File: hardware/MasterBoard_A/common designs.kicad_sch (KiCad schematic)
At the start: 48 parts, among them J12 Conn_01x05_Pin, J13 Main Current Hall Effect Sens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, J14 Conn_02x03_Top_Bottom, Q20 MMBT5550L, Q21 MMBT5550L, Q22 MMBT5550L, U11 IPD70R, U24 LM74502, U25 IPD70R, U42 IPD70R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

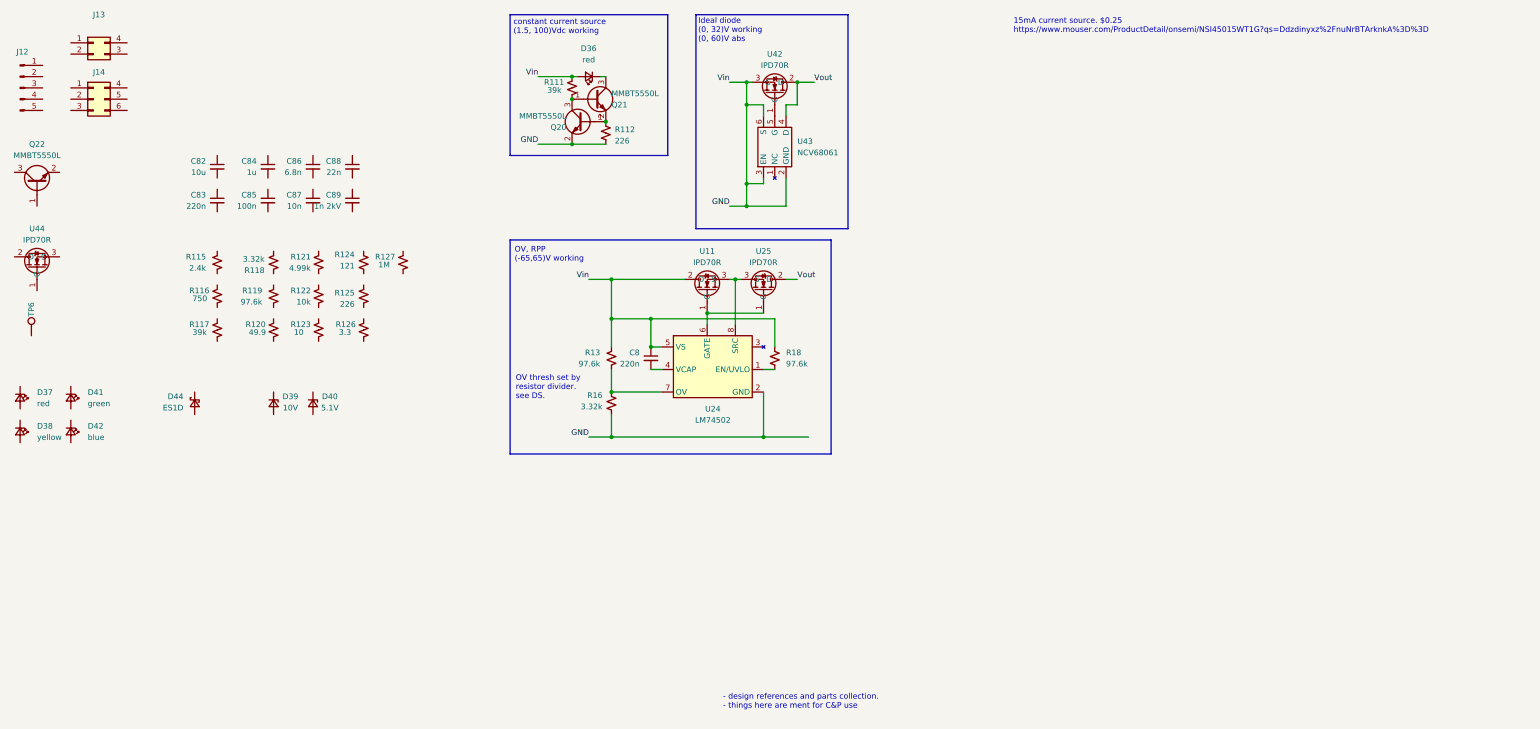
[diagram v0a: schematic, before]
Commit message: better-ified power stuff. new costing program
handy new costing program for kicad. just c&p symbols directly from kicad into it and itll dump out the BOM cost of what ever you gave it
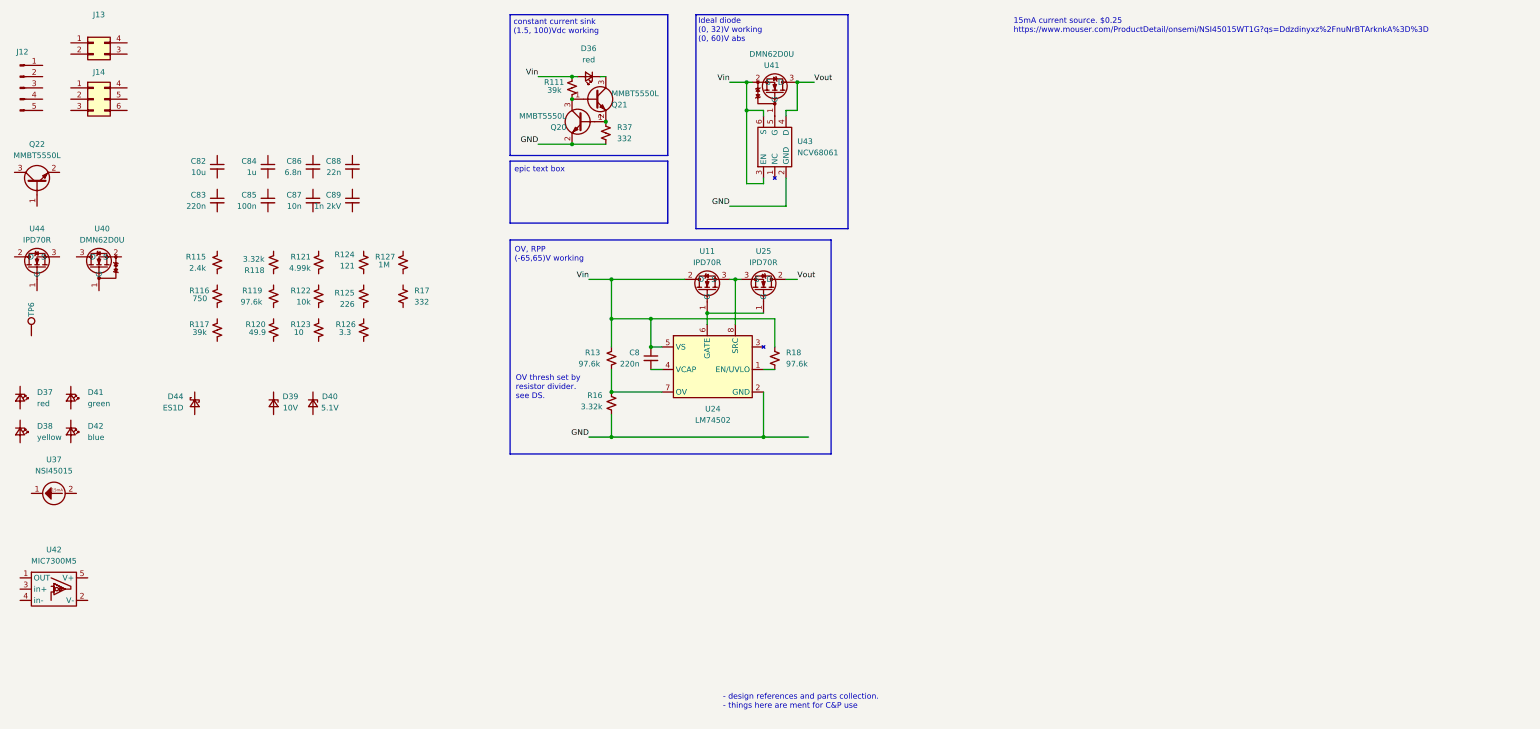
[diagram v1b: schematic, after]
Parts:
- removed R112: 226, Resistor_SMD:R_0805_2012Metric_Pad1.20x1.40mm_HandSolder, symbol Device:R_Small_US
- removed U42: IPD70R, Package_TO_SOT_SMD:TO-252-2, symbol zzLocalLibrary:IPD70R
- added R17, R37: 332, Resistor_SMD:R_1206_3216Metric_Pad1.30x1.75mm_HandSolder, symbol Device:R_Small_US
- added U37: NSI45015, Diode_SMD:D_SOD-123, symbol zzLocalLibrary:NSI45015
- added U40, U41: DMN62D0U, Package_TO_SOT_SMD:SOT-23_Handsoldering, symbol zzLocalLibrary:DMN62D0U
- added U42: MIC7300M5, Package_TO_SOT_SMD:TSOT-23-5_HandSoldering, symbol zzLocalLibrary:MIC7300M5
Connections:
- net GND: now also R37.1; no longer C8.1, D36.2 (A), R111.2, R13.2, R18.2, U11.2 (D), U24.5 (VS), U43.3 (EN), U43.6 (S)
- net Vout: now also U41.3 (D)
- net at U43.5 (G): now also U41.1 (G)
- net at Q20.1 (B), Q21.2 (E): now also R37.2
- new net Vin: C8.1, D36.2 (A), R111.2, R13.2, R18.2, U11.2 (D), U24.5 (VS), U41.2 (S), U43.3 (EN), U43.6 (S)
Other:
- note added: "constant current sink (1.5, 100)Vdc working"
- note removed: "constant current source (1.5, 100)Vdc working"

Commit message: near final
missing direct MCU connections, pin map excel sheet needs piddled with. schematic needs reviewed
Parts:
- added U12: MCP9700x-ETT, Package_TO_SOT_SMD:SOT-23-3, symbol Sensor_Temperature:MCP9700x-ETT
- added U49: TLV713185PDBV, Package_TO_SOT_SMD:SOT-23-5, symbol Regulator_Linear:TLV713185PDBV
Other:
- note added: "- does not go on board. is for convenience - design references and parts collection. - things here are ment for C&P use"
- note removed: "- design references and parts collection. - things here are ment for C&P use"
- note removed: "15mA current source. $0.25 https://www.mouser.com/ProductDetail/onsemi/NSI45015WT1G?qs=Ddzdinyxz%2FnuNrBTArknkA%3D%3D"
- moved on the sheet: C8, R13, R16, R18, U11, U24, U25, U41, U42, U43

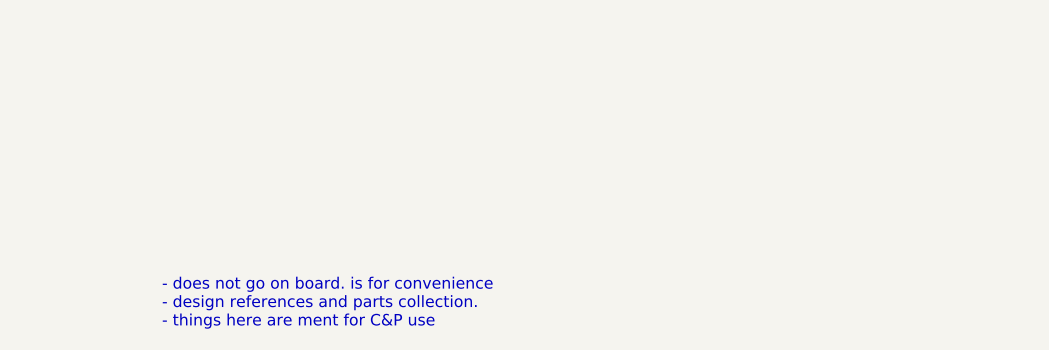
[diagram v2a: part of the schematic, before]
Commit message: one must have hope
eyeballed the ethernet transmission lines, i think it'll work. absolute pain without using footprints smaller than 0805 but it think itll be fine. also shuffled together the PWM sig bank
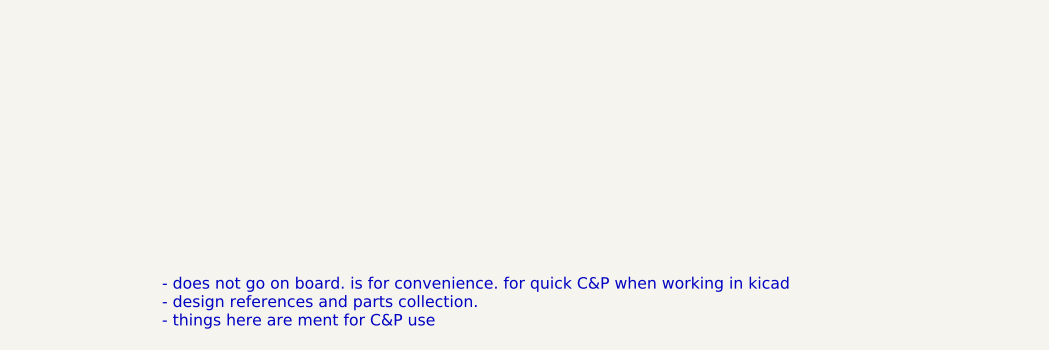
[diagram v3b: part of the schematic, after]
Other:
- note added: "- does not go on board. is for convenience. for quick C&P when working in kicad - design references and parts collection. - things here are ment for C&P use"
- note removed: "- does not go on board. is for convenience - design references and parts collection. - things here are ment for C&P use"

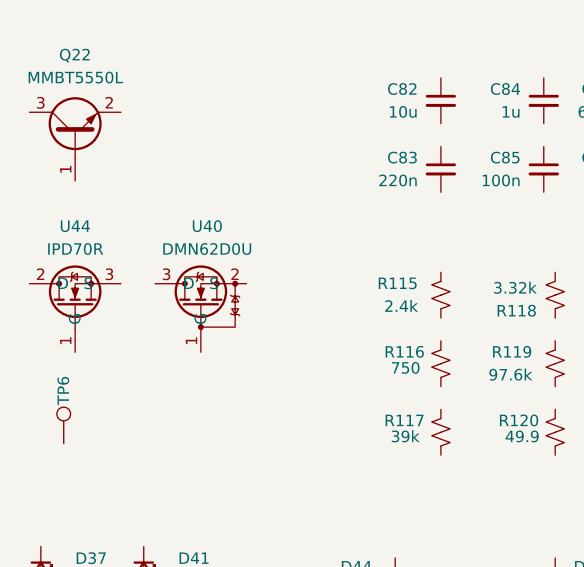
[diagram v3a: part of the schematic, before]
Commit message: partial layout of psu
pdn about to look like a mine field
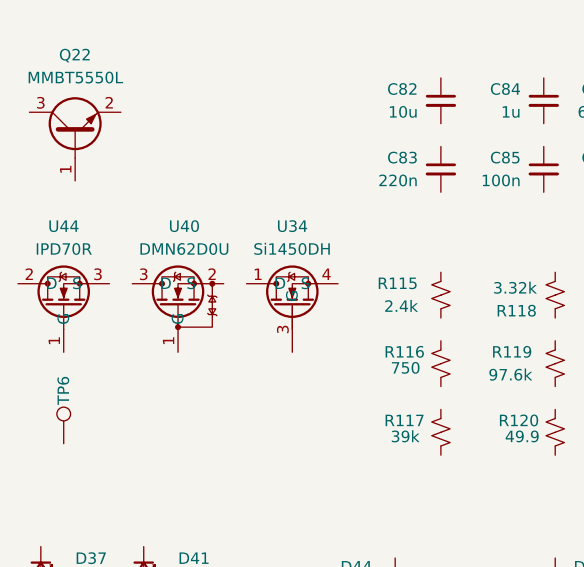
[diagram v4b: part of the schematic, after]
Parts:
- added U34: Si1450DH, Package_TO_SOT_SMD:SOT-363_SC-70-6_Handsoldering, symbol zzLocalLibrary:Si1480DH
- U43: footprint Package_SO:TSOP-6_1.65x3.05mm_P0.95mm -> Package_TO_SOT_SMD:TSOT-23-6
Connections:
- new net: U34.1 (D), U34.2 (D), U34.5 (D), U34.6 (D)
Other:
- moved on the sheet: U40, U44
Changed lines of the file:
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@@
 	)
 	(symbol
+		(lib_id "zzLocalLibrary:Si1480DH")
+		(at 48.26 66.04 0)
+		(unit 1)
+		(exclude_from_sim no)
+		(in_bom yes)
+		(on_board yes)
+		(dnp no)
+		(fields_autoplaced yes)
+		(property "Reference" "U34"
+			(at 48.26 63.5 0)
+			(effects
+				(font
+					(size 1.27 1.27)
+				)
+			)
+		)
+		(property "Value" "Si1450DH"
+			(at 48.26 66.04 0)
+			(effects
+				(font
+					(size 1.27 1.27)
+				)
+			)
+		)
+		(property "Footprint" "Package_TO_SOT_SMD:SOT-363_SC-70-6_Handsoldering"
+			(at 48.26 66.04 0)
+			(effects
+				(font
+					(size 1.27 1.27)
+				)
+				(hide yes)
+			)
+		)
+		(property "Datasheet" "https://www.vishay.com/docs/67327/si1480dh.pdf"
+			(at 48.26 66.04 0)
+			(effects
+				(font
+					(size 1.27 1.27)
+				)
+				(hide yes)
+			)
+		)
+		(property "Description" ""
+			(at 48.26 66.04 0)
+			(effects
+				(font
+					(size 1.27 1.27)
+				)
+				(hide yes)
+			)
+		)
+		(property "specs" "2.6A cont, 200mOhm, 100Vds, +-20Vgs, -55C, +150C"
+			(at 48.26 66.04 0)
+			(effects
+				(font
+					(size 1.27 1.27)
+				)
+				(hide yes)
+			)
+		)
+		(property "mouser" "https://www.mouser.com/ProductDetail/Vishay-Siliconix/SI1480DH-T1-BE3?qs=zW32dvEIR3scWOH7DHfYCg%3D%3D"
+			(at 48.26 66.04 0)
+			(effects
+				(font
+					(size 1.27 1.27)
+				)
+				(hide yes)
+			)
+		)
+		(property "unit x10" "0.274"
+			(at 48.26 66.04 0)
+			(effects
+				(font
+					(size 1.27 1.27)
+				)
+				(hide yes)
+			)
+		)
+		(property "unit x1" "0.34"
+			(at 48.26 66.04 0)
+			(effects
+				(font
+					(size 1.27 1.27)
+				)
+				(hide yes)
+			)
+		)
+		(pin "5"
+		)
+		(pin "4"
+		)
+		(pin "3"
+		)
+		(pin "2"
+		)
+		(pin "1"
+		)
+		(pin "6"
+		)
+		(instances
+			(project "MasterBoard_A"
+				(path "/20ac6af0-79b5-4ba6-aad3-75081d02c913/e647e6c7-d2c9-4086-bd05-45f6d07d327b"
+					(reference "U34")
+					(unit 1)
+				)
+			)
+		)
+	)
+	(symbol
 		(lib_id "zzLocalLibrary:NSI45015")
 		(at 27.94 121.92 0)
@@
 	(symbol
 		(lib_id "zzLocalLibrary:DMN62D0U")
-		(at 38.1 69.85 90)
+		(at 35.56 69.85 90)
 		(unit 1)
 		(exclude_from_sim no)
@@
 		(fields_autoplaced yes)
 		(property "Reference" "U40"
-			(at 38.7985 63.5 90)
+			(at 36.2585 63.5 90)
 			(effects
 				(font
@@
 		)
 		(property "Value" "DMN62D0U"
-			(at 38.7985 66.04 90)
+			(at 36.2585 66.04 90)
 			(effects
 				(font
@@
 		)
 		(property "Footprint" "Package_TO_SOT_SMD:SOT-23_Handsoldering"
-			(at 38.1 69.85 0)
+			(at 35.56 69.85 0)
 			(effects
 				(font
@@
 		)
 		(property "Datasheet" "https://4donline.ihs.com/images/VipMasterIC/IC/DIOD/DIOD-S-A0002833665/DIOD-S-A0002833270-1.pdf?hkey=CECEF36DEECDED6468708AAF2E19C0C6"
-			(at 38.1 69.85 0)
+			(at 35.56 69.85 0)
 			(effects
 				(font
@@
 		)
 		(property "Description" ""
-			(at 38.1 69.85 0)
+			(at 35.56 69.85 0)
 			(effects
 				(font
@@
 		)
 		(property "specs" "500mVth, 60Vds, +-20Vgs, 380mA cont, 2 ohm, 590mW"
-			(at 38.1 69.85 0)
+			(at 35.56 69.85 0)
 			(effects
 				(font
@@
 		)
 		(property "mouser" "https://www.mouser.com/ProductDetail/Diodes-Incorporated/DMN62D0U-7?qs=ANipbH0jDF1YQ7DvWYjVRw%3D%3D"
-			(at 38.1 69.85 0)
+			(at 35.56 69.85 0)
 			(effects
 				(font
@@
 		)
 		(property "unit x10" "0.102"
-			(at 38.1 69.85 0)
+			(at 35.56 69.85 0)
 			(effects
 				(font
@@
 		)
 		(property "unit x1" "0.12"
-			(at 38.1 69.85 0)
+			(at 35.56 69.85 0)
 			(effects
 				(font
@@
 		)
 		(property "Sim.Pins" ""
-			(at 38.1 69.85 90)
+			(at 35.56 69.85 90)
 			(effects
 				(font
@@
 		)
 		(property "note" ""
-			(at 38.1 69.85 90)
+			(at 35.56 69.85 90)
 			(effects
 				(font
@@
 			)
 		)
-		(property "Footprint" "Package_SO:TSOP-6_1.65x3.05mm_P0.95mm"
+		(property "Footprint" "Package_TO_SOT_SMD:TSOT-23-6"
 			(at 185.42 44.45 0)
 			(effects
@@
 	(symbol
 		(lib_id "zzLocalLibrary:IPD70R")
-		(at 24.13 69.85 90)
+		(at 22.86 69.85 90)
 		(unit 1)
 		(exclude_from_sim no)
@@
 		(fields_autoplaced yes)
 		(property "Reference" "U44"
-			(at 24.13 63.5 90)
+			(at 22.86 63.5 90)
 			(effects
 				(font
@@
 		)
 		(property "Value" "IPD70R"
-			(at 24.13 66.04 90)
+			(at 22.86 66.04 90)
 			(effects
 				(font
@@
 		)
 		(property "Footprint" "Package_TO_SOT_SMD:TO-252-2"
-			(at 24.13 69.85 0)
+			(at 22.86 69.85 0)
 			(effects
 				(font
@@
 		)
 		(property "Datasheet" ""
-			(at 24.13 69.85 0)
+			(at 22.86 69.85 0)
 			(effects
 				(font
@@
 		)
 		(property "Description" "nmos, 300mOhm, 700Vdc, 2.5 [16,-16]Vgs, -40C,+150C"
-			(at 24.13 69.85 0)
+			(at 22.86 69.85 0)
 			(effects
 				(font
@@
 		)
 		(property "mouser" "https://www.mouser.com/ProductDetail/Infineon-Technologies/IPD70R360P7SAUMA1?qs=KuGazDKa6A7NZ4kbDDKXAg%3D%3D"
-			(at 24.13 69.85 0)
+			(at 22.86 69.85 0)
 			(effects
 				(font
@@
 		)
 		(property "unit x10" "0.482"
-			(at 24.13 69.85 0)
+			(at 22.86 69.85 0)
 			(effects
 				(font
@@
 		)
 		(property "unit x1" "0.55"
-			(at 24.13 69.85 0)
+			(at 22.86 69.85 0)
 			(effects
 				(font
@@
 		)
 		(property "Sim.Pins" ""
-			(at 24.13 69.85 90)
+			(at 22.86 69.85 90)
 			(effects
 				(font
@@
 		)
 		(property "note" ""
-			(at 24.13 69.85 90)
+			(at 22.86 69.85 90)
 			(effects
 				(font

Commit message: up to date meta sheet and made release files
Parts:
- C85: mouser https://www.mouser.com/ProductDetail/Walsin/1206B104K251CT?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 -> https://www.mouser.com/ProductDetail/Walsin/1206B104K201CT?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; specs 100nF, 250VDC, X7R, 10%, -55C, +125C -> 100nF, 200VDC, X7R, 10%, -55C, +125C; unit x1 (none) -> 0.11; unit x10 0.042 -> 0.045
- J12: mouser (none) -> https://www.mouser.com/ProductDetail/Molex/43650-0500?qs=6R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
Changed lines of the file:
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@@
 			)
 		)
-		(property "mouser" "https://www.mouser.com/ProductDetail/Walsin/1206B104K251CT?qs=fIkAfuXiAQKkmX5niKUTKw%3D%3D"
+		(property "mouser" "https://www.mouser.com/ProductDetail/Walsin/1206B104K201CT?qs=fIkAfuXiAQKvqIFf8la7zg%3D%3D"
 			(at 76.2 57.15 0)
 			(effects
@@
 			)
 		)
-		(property "specs" "100nF, 250VDC, X7R, 10%, -55C, +125C"
+		(property "specs" "100nF, 200VDC, X7R, 10%, -55C, +125C"
 			(at 76.2 57.15 0)
 			(effects
@@
 			)
 		)
-		(property "unit x10" "0.042"
+		(property "unit x10" "0.045"
 			(at 76.2 57.15 0)
 			(effects
@@
 		)
 		(property "note" ""
+			(at 76.2 57.15 0)
+			(effects
+				(font
+					(size 1.27 1.27)
+				)
+				(hide yes)
+			)
+		)
+		(property "unit x1" "0.11"
 			(at 76.2 57.15 0)
 			(effects
@@
 			(at 20.32 31.75 0)
 			(effects
+				(font
+					(size 1.27 1.27)
+				)
+				(hide yes)
+			)
+		)
+		(property "mouser" "https://www.mouser.com/ProductDetail/Molex/43650-0500?qs=6RXNyJqNVR5CcLURnhE2cQ%3D%3D"
+			(at 20.32 31.75 0)
+			(effects
